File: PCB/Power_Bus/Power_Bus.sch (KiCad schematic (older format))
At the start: 39 parts, among them J1 CONN_01X01, J2 CONN_01X01, J3 CONN_01X01, J4 CONN_01X01, Q2 TP0610T, Q4 TP0610T, U1 ATMEGA128-16AU, Y1 Crystal

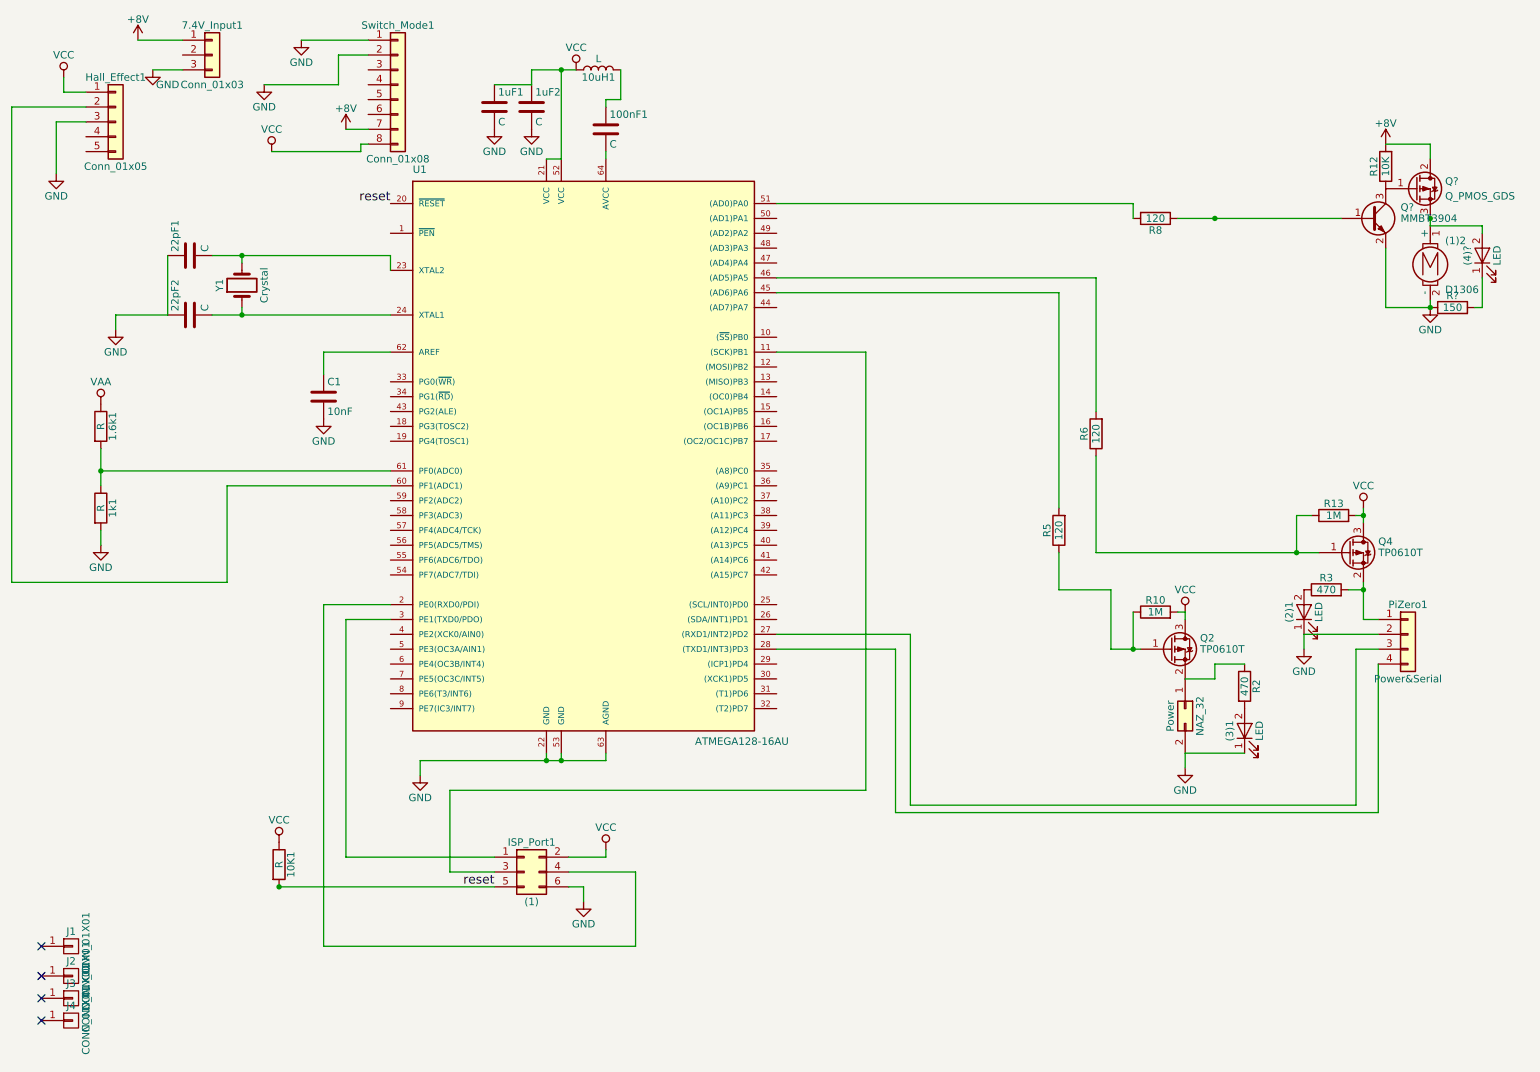
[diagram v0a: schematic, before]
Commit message: added team name to silkscreen
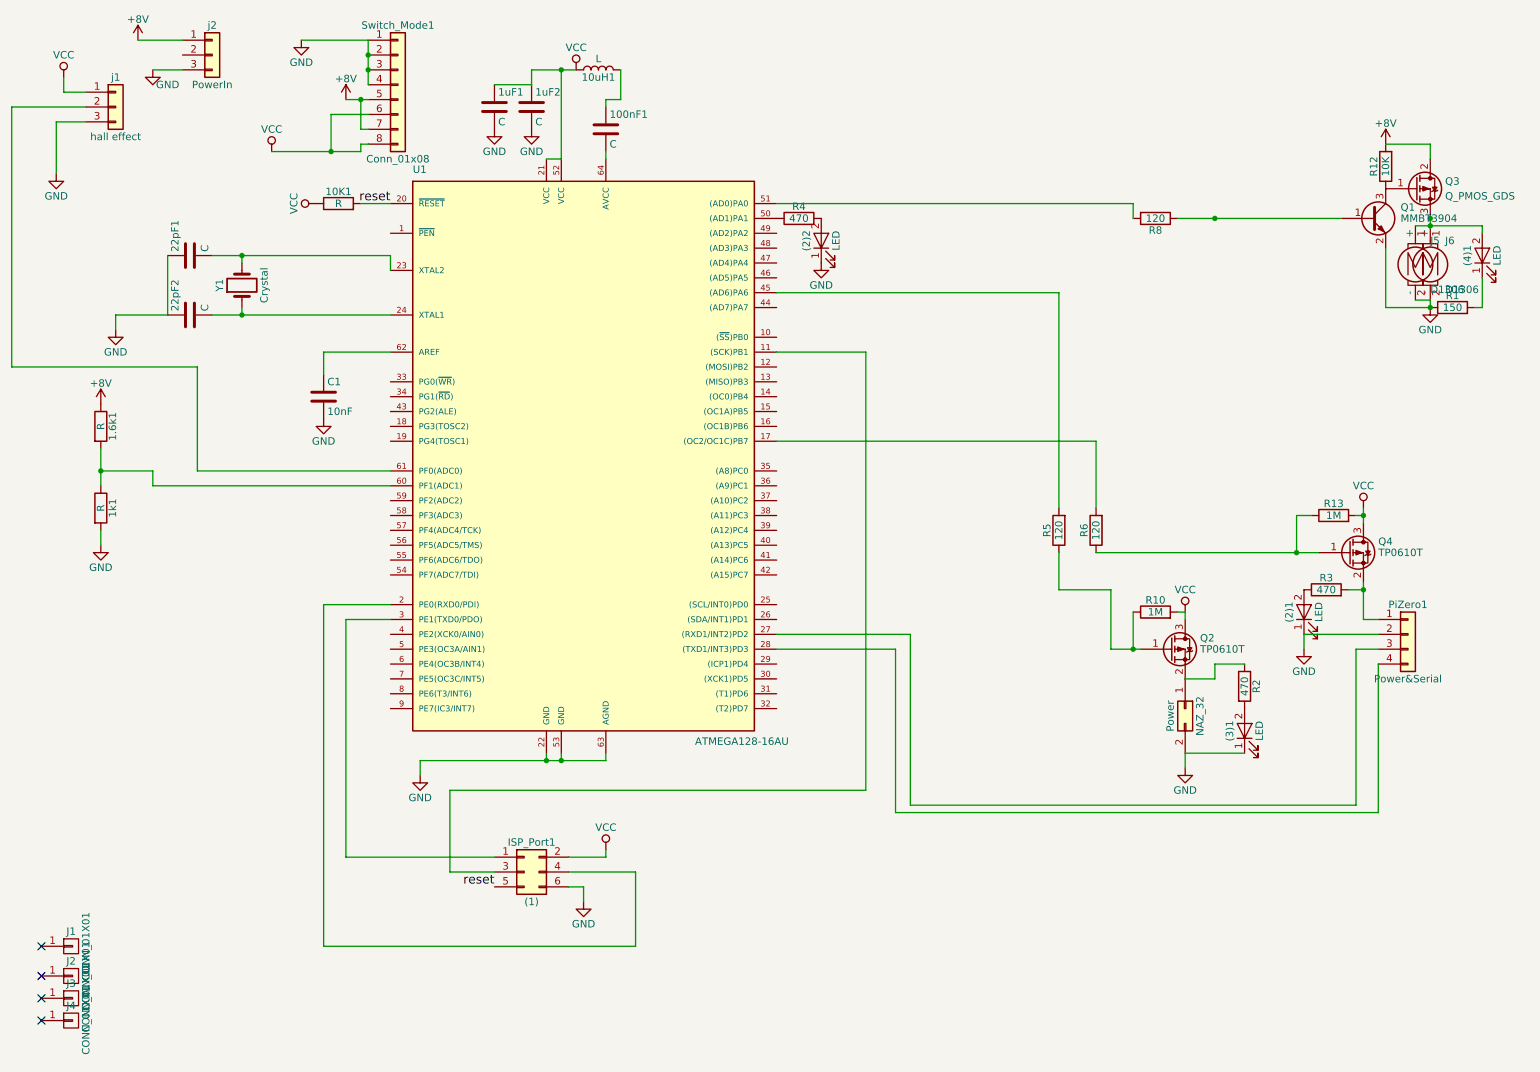
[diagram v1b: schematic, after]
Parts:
- removed (1)2: D1306, Pin_Headers:Pin_Header_Straight_1x02_Pitch2.54mm, symbol Motor_DC_ALT
- removed Hall_Effect1: Conn_01x05, Pin_Headers:Pin_Header_Straight_1x05_Pitch2.54mm, symbol Conn_01x05
- added (2)2: LED, LEDs:LED_0603_HandSoldering, symbol LED
- added J5, J6: D1306, Connectors_JST:JST_EH_S02B-EH_02x2.50mm_Angled, symbol Motor_DC_ALT
- added R4: 470, Resistors_SMD:R_0805_HandSoldering, symbol R
- added j1: hall effect, Pin_Headers:Pin_Header_Straight_1x03_Pitch2.54mm, symbol Conn_01x03
- (2)1, (3)1: footprint LEDs:LED_D3.0mm -> LEDs:LED_0603_HandSoldering
- (4)1: renamed from (4)?; footprint LEDs:LED_D3.0mm -> LEDs:LED_0603_HandSoldering
- NAZ_32: footprint Pin_Headers:Pin_Header_Straight_2x01_Pitch2.54mm -> Connectors_JST:JST_EH_S02B-EH_02x2.50mm_Angled
- Q3: renamed from Q?; footprint (none) -> TO_SOT_Packages_SMD:TO-252-3_TabPin2
- j2: renamed from 7.4V_Input1; value Conn_01x03 -> PowerIn; footprint Pin_Headers:Pin_Header_Straight_1x03_Pitch2.54mm -> Connectors_JST:JST_EH_S03B-EH_03x2.50mm_Angled
- gave numbers to parts that had none: 2
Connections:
- net VAA is gone; now on net +8V: 1.6k1.1
- net +8V: now also Switch_Mode1.5 (Pin_5)
- net GND: now also Switch_Mode1.3 (Pin_3), Switch_Mode1.4 (Pin_4), (2)2.1 (K), J5.2 (-), J6.2 (-), j1.3 (Pin_3)
- net VCC: now also Switch_Mode1.6 (Pin_6), j1.1 (Pin_1)
- net at U1.17 ((OC2/OC1C)PB7): now also R6.2
- net at U1.46 ((AD5)PA5): no longer R6.2
- net at U1.50 ((AD1)PA1): now also R4.1
- net at U1.60 (PF1(ADC1)): now also 1.6k1.2, 1k1.1
- net at (4)1.2 (A), Q3.3 (S): now also J5.1 (+), J6.1 (+)
- new net: U1.61 (PF0(ADC0)), j1.2 (Pin_2)
- new net: (2)2.2 (A), R4.2
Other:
- moved on the sheet: 10K1, R6

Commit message: rotate mosfets in sch. not in the pcb
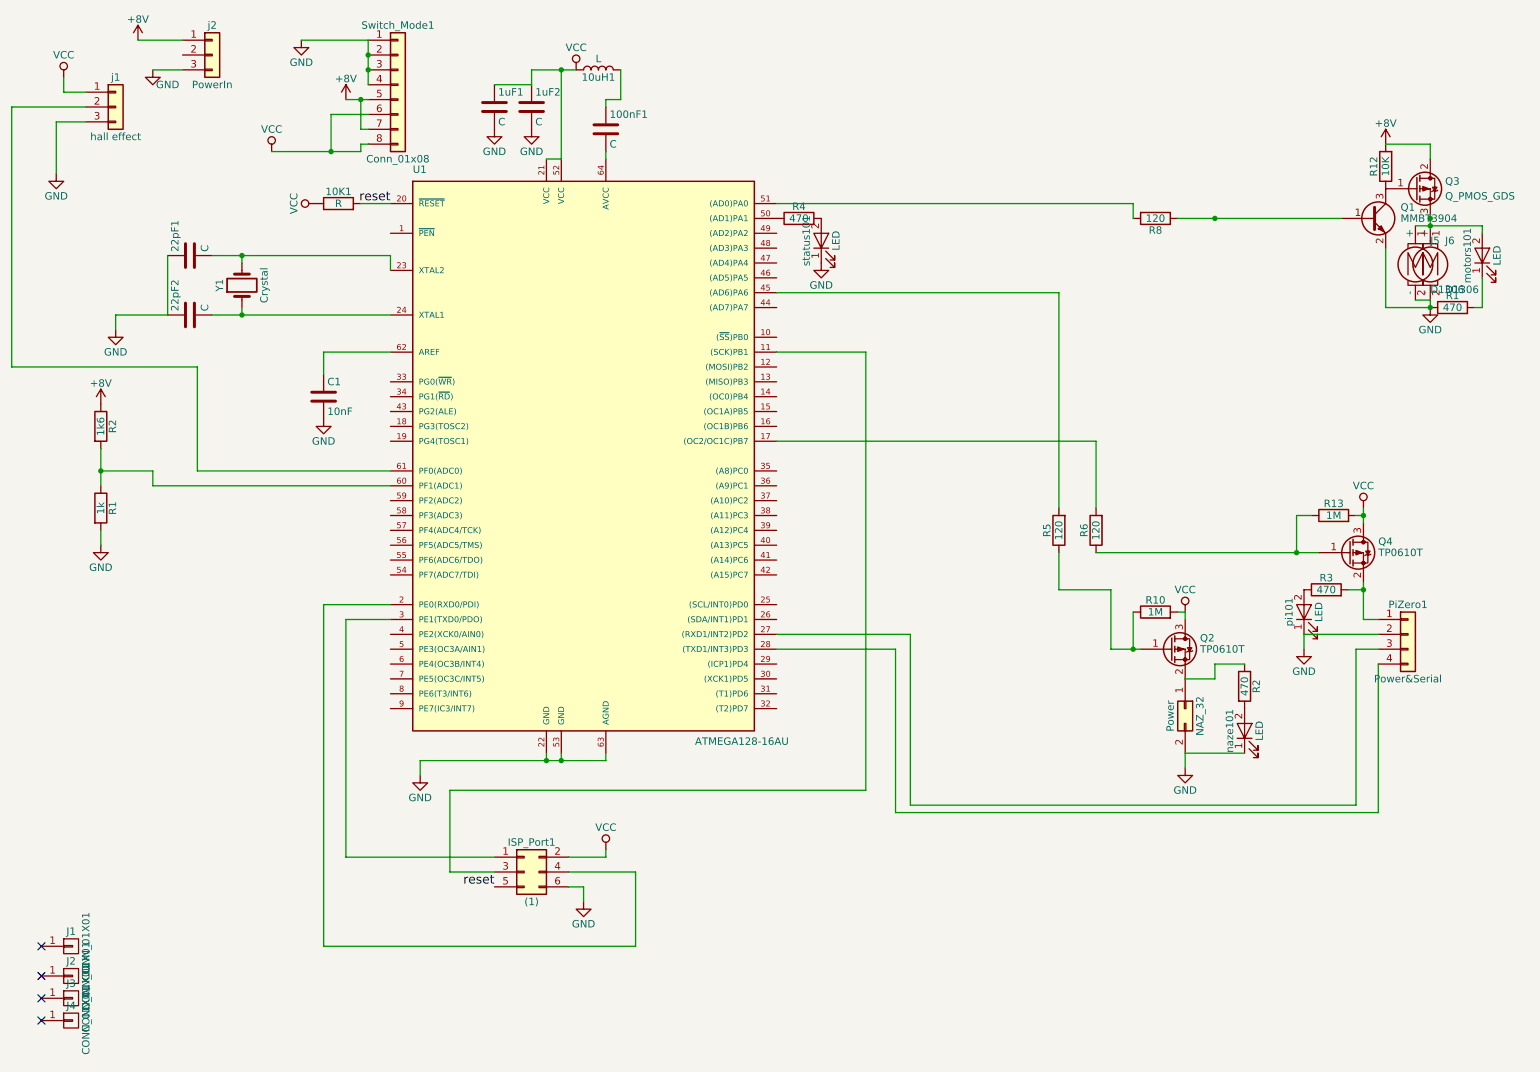
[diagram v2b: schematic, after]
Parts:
- R1: renamed from 1k1; value R -> 1k
- R1: value 150 -> 470
- R2: renamed from 1.6k1; value R -> 1k6
- renumbered (4)1 to motors101, (3)1 to naze101, (2)1 to pi101, (2)2 to status101
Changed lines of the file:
@@
 $EndComp
 $Comp
-L LED (2)1
+L LED pi101
 U 1 1 5AA926E0
 P 9250 4650
-F 0 "(2)1" H 9250 4750 50  0000 C CNN
+F 0 "pi101" H 9250 4750 50  0000 C CNN
 F 1 "LED" H 9250 4550 50  0000 C CNN
 F 2 "LEDs:LED_0603_HandSoldering" H 9250 4650 50  0001 C CNN
@@
 $EndComp
 $Comp
-L LED (3)1
+L LED naze101
 U 1 1 5AA9276D
 P 8850 5450
-F 0 "(3)1" H 8850 5550 50  0000 C CNN
+F 0 "naze101" H 8850 5550 50  0000 C CNN
 F 1 "LED" H 8850 5350 50  0000 C CNN
 F 2 "LEDs:LED_0603_HandSoldering" H 8850 5450 50  0001 C CNN
@@
 $EndComp
 $Comp
-L R 1.6k1
+L R R2
 U 1 1 5AD22F50
 P 1150 3400
-F 0 "1.6k1" V 1230 3400 50  0000 C CNN
-F 1 "R" V 1150 3400 50  0000 C CNN
+F 0 "R2" V 1230 3400 50  0000 C CNN
+F 1 "1k6" V 1150 3400 50  0000 C CNN
 F 2 "Resistors_SMD:R_0805_HandSoldering" V 1080 3400 50  0001 C CNN
 F 3 "" H 1150 3400 50  0001 C CNN
@@
 $EndComp
 $Comp
-L R 1k1
+L R R1
 U 1 1 5AD233BA
 P 1150 3950
-F 0 "1k1" V 1230 3950 50  0000 C CNN
-F 1 "R" V 1150 3950 50  0000 C CNN
+F 0 "R1" V 1230 3950 50  0000 C CNN
+F 1 "1k" V 1150 3950 50  0000 C CNN
 F 2 "Resistors_SMD:R_0805_HandSoldering" V 1080 3950 50  0001 C CNN
 F 3 "" H 1150 3950 50  0001 C CNN
@@
 reset
 $Comp
-L LED (4)1
+L LED motors101
 U 1 1 5AE770DD
 P 10450 2250
-F 0 "(4)1" H 10450 2350 50  0000 C CNN
+F 0 "motors101" H 10450 2350 50  0000 C CNN
 F 1 "LED" H 10450 2150 50  0000 C CNN
 F 2 "LEDs:LED_0603_HandSoldering" H 10450 2250 50  0001 C CNN
@@
 P 10250 2600
 F 0 "R1" V 10330 2600 50  0000 C CNN
-F 1 "150" V 10250 2600 50  0000 C CNN
+F 1 "470" V 10250 2600 50  0000 C CNN
 F 2 "Resistors_SMD:R_0805_HandSoldering" V 10180 2600 50  0001 C CNN
 F 3 "" H 10250 2600 50  0001 C CNN
@@
 $EndComp
 $Comp
-L LED (2)2
+L LED status101
 U 1 1 5AE87D1E
 P 6000 2150
-F 0 "(2)2" H 6000 2250 50  0000 C CNN
+F 0 "status101" H 6000 2250 50  0000 C CNN
 F 1 "LED" H 6000 2050 50  0000 C CNN
 F 2 "LEDs:LED_0603_HandSoldering" H 6000 2150 50  0001 C CNN
